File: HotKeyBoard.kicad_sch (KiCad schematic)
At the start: 397 parts, among them J1 Conn_01x04_Pin, J2 Conn_01x20_Pin, J3 Conn_01x20_Pin, J4 Conn_01x02_Socket, J5 Conn_01x02_Socket, J6 Conn_01x02_Socket, Q1 IRLZ34N, Q2 IRLZ34N, Q3 IRLZ34N, SW1 SW_Push, SW10 SW_Push, SW11 SW_Push, SW12 SW_Push, SW13 SW_Push, SW14 SW_Push, SW15 SW_Push, SW16 SW_Push, SW17 SW_Push, SW18 SW_Push, SW19 SW_Push, SW2 SW_Push, SW20 SW_Push, SW21 SW_Push, SW22 SW_Push, SW23 SW_Push, SW24 SW_Push, SW25 SW_Push, SW26 SW_Push, SW27 SW_Push, SW28 SW_Push, SW29 SW_Push, SW3 SW_Push, SW30 SW_Push, SW31 SW_Push, SW32 SW_Push, SW33 SW_Push, SW34 SW_Push, SW35 SW_Push, SW36 SW_Push, SW37 SW_Push, SW38 SW_Push, SW39 SW_Push, SW4 SW_Push, SW40 SW_Push, SW41 SW_Push, SW42 SW_Push, SW43 SW_Push, SW44 SW_Push, SW45 SW_Push, SW46 SW_Push, SW47 SW_Push, SW48 SW_Push, SW49 SW_Push, SW5 SW_Push, SW50 SW_Push, SW51 SW_Push, SW52 SW_Push, SW53 SW_Push, SW54 SW_Push, SW55 SW_Push, SW56 SW_Push, SW57 SW_Push, SW58 SW_Push, SW59 SW_Push, SW6 SW_Push, SW60 SW_Push, SW61 SW_Push, SW62 SW_Push, SW63 SW_Push, SW64 SW_Push, SW65 SW_Push, SW66 SW_Push, SW67 SW_Push, SW68 SW_Push, SW69 SW_Push, SW7 SW_Push, SW70 SW_Push, SW71 SW_Push, SW72 SW_Push, SW76 SW_Push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

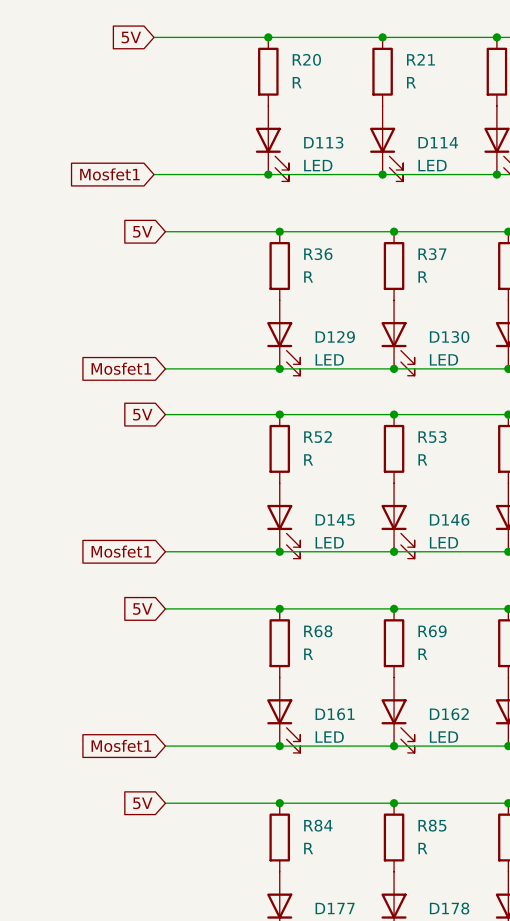
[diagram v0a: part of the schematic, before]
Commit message: Rewired leds
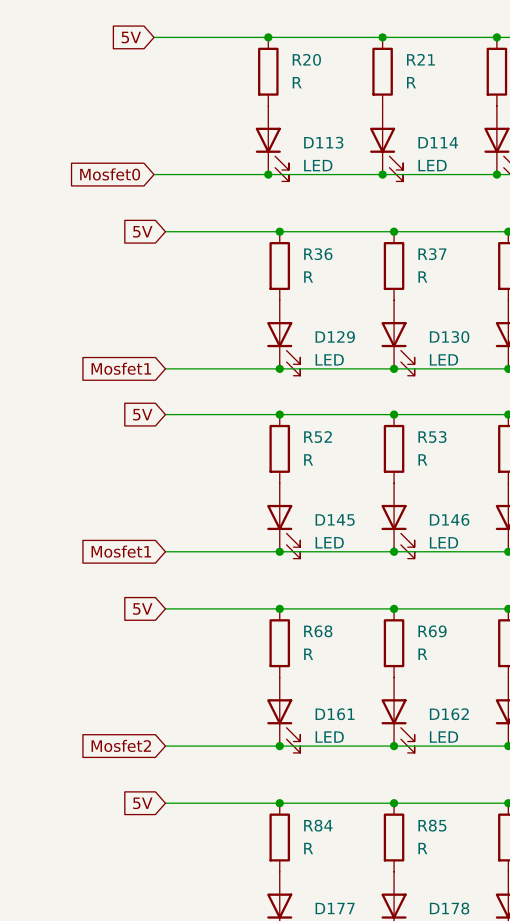
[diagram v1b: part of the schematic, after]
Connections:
- net Mosfet0: now also D113.1 (K), D114.1 (K), D115.1 (K), D116.1 (K), D117.1 (K), D118.1 (K), D119.1 (K), D120.1 (K), D121.1 (K), D122.1 (K), D123.1 (K), D124.1 (K), D125.1 (K), D126.1 (K), D127.1 (K), D128.1 (K)
- net Mosfet1: no longer D113.1 (K), D114.1 (K), D115.1 (K), D116.1 (K), D117.1 (K), D118.1 (K), D119.1 (K), D120.1 (K), D121.1 (K), D122.1 (K), D123.1 (K), D124.1 (K), D125.1 (K), D126.1 (K), D127.1 (K), D128.1 (K), D161.1 (K), D162.1 (K), D163.1 (K), D164.1 (K), D165.1 (K), D166.1 (K), D167.1 (K), D168.1 (K), D169.1 (K), D170.1 (K), D171.1 (K), D172.1 (K), D173.1 (K), D174.1 (K), D175.1 (K), D176.1 (K)
- net Mosfet2: now also D161.1 (K), D162.1 (K), D163.1 (K), D164.1 (K), D165.1 (K), D166.1 (K), D167.1 (K), D168.1 (K), D169.1 (K), D170.1 (K), D171.1 (K), D172.1 (K), D173.1 (K), D174.1 (K), D175.1 (K), D176.1 (K)
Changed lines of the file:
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@@
     )
   )
-  (global_label "Mosfet1" (shape input) (at 62.23 236.22 180)
+  (global_label "Mosfet0" (shape input) (at 62.23 236.22 180)
     (effects (font (size 1.27 1.27)) (justify right))
     (property "Intersheetrefs" "${INTERSHEET_REFS}" (at 62.23 236.22 0)
@@
     )
   )
-  (global_label "Mosfet1" (shape input) (at 63.5 299.72 180)
+  (global_label "Mosfet2" (shape input) (at 63.5 299.72 180)
     (effects (font (size 1.27 1.27)) (justify right))
     (property "Intersheetrefs" "${INTERSHEET_REFS}" (at 63.5 299.72 0)

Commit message: Changed led resistor to smaller value to give pwm control more range to play with
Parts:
- R10, R11, R12, R13, R14, R15, R16, R17, R18, R19, R20, R21, R22, R23, R24, R25, R26, R27, R28, R29, R30, R31, R32, R33, R34, R35, R36, R37, R38, R39, R4, R40, R41, R42, R43, R44, R45, R46, R47, R48, R49, R5, R50, R51, R52, R53, R54, R55, R56, R57, R58, R59, R6, R60, R61, R62, R63, R64, R65, R66, R67, R68, R69, R7, R70, R71, R72, R73, R74, R75, R76, R77, R78, R79, R8, R80, R81, R82, R83, R84, R85, R86, R87, R88, R89, R9, R90, R91, R92, R93, R94, R95, R96, R97, R98, R99: LCSC C881395 -> C101269

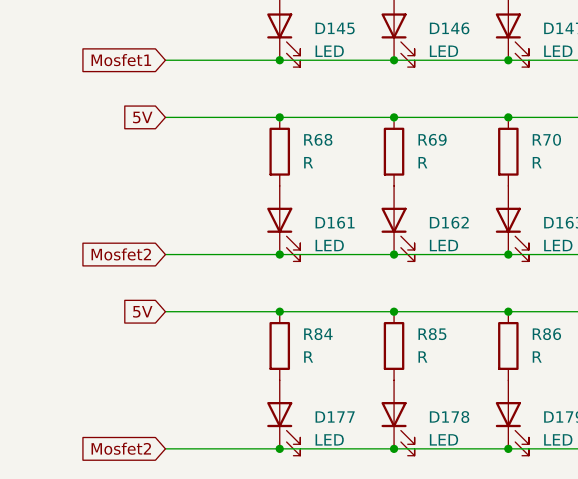
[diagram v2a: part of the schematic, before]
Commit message: Added 0ohm resistor before the last led row in order to be able to turn it off
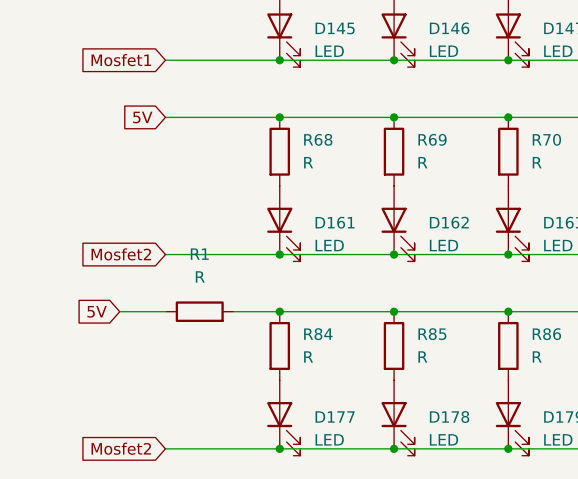
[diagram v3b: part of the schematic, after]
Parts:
- added R1: R, Resistor_THT:R_Axial_DIN0204_L3.6mm_D1.6mm_P5.08mm_Horizontal, symbol Device:R
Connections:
- net 5V: now also R1.1; no longer R84.1, R85.1, R86.1, R87.1, R88.1, R89.1, R90.1, R91.1, R92.1, R93.1, R94.1, R95.1, R96.1, R97.1, R98.1, R99.1
- new net: R1.2, R84.1, R85.1, R86.1, R87.1, R88.1, R89.1, R90.1, R91.1, R92.1, R93.1, R94.1, R95.1, R96.1, R97.1, R98.1, R99.1
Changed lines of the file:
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@@
   (junction (at 485.14 104.14) (diameter 0) (color 0 0 0 0)
   )
-  (junction (at 76.2 306.07) (diameter 0) (color 0 0 0 0)
-  )
   (junction (at 163.83 236.22) (diameter 0) (color 0 0 0 0)
   )
@@
   (junction (at 228.6 306.07) (diameter 0) (color 0 0 0 0)
   )
+  (junction (at 76.2 306.07) (diameter 0) (color 0 0 0 0)
+  )
   (junction (at 353.06 124.46) (diameter 0) (color 0 0 0 0)
   )
@@
     (stroke (width 0) (type default))
   )
+  (wire (pts (xy 58.42 306.07) (xy 63.5 306.07))
+    (stroke (width 0) (type default))
+  )
   (wire (pts (xy 486.41 284.48) (xy 486.41 281.94))
     (stroke (width 0) (type default))
@@
     (stroke (width 0) (type default))
   )
-  (wire (pts (xy 63.5 306.07) (xy 76.2 306.07))
-    (stroke (width 0) (type default))
-  )
   (polyline (pts (xy 521.97 207.01) (xy 528.32 207.01))
     (stroke (width 0) (type default))
@@
     (stroke (width 0) (type default))
   )
+  (wire (pts (xy 71.12 306.07) (xy 76.2 306.07))
+    (stroke (width 0) (type default))
+  )
   (wire (pts (xy 139.7 321.31) (xy 152.4 321.31))
     (stroke (width 0) (type default))
@@
     )
   )
-  (global_label "5V" (shape input) (at 63.5 306.07 180) (fields_autoplaced)
+  (global_label "5V" (shape input) (at 58.42 306.07 180) (fields_autoplaced)
     (effects (font (size 1.27 1.27)) (justify right))
-    (property "Intersheetrefs" "${INTERSHEET_REFS}" (at 58.2167 306.07 0)
+    (property "Intersheetrefs" "${INTERSHEET_REFS}" (at 53.1367 306.07 0)
       (effects (font (size 1.27 1.27)) (justify right) hide)
     )
@@
         )
       )
+    )
+  )
+  (symbol (lib_id "Device:R") (at 67.31 306.07 90) (unit 1)
+    (in_bom yes) (on_board yes) (dnp no) (fields_autoplaced)
+    (property "Reference" "R1" (at 67.31 299.72 90)
+      (effects (font (size 1.27 1.27)))
+    )
+    (property "Value" "R" (at 67.31 302.26 90)
+      (effects (font (size 1.27 1.27)))
+    )
+    (property "Footprint" "Resistor_THT:R_Axial_DIN0204_L3.6mm_D1.6mm_P5.08mm_Horizontal" (at 67.31 307.848 90)
+      (effects (font (size 1.27 1.27)) hide)
+    )
+    (property "Datasheet" "~" (at 67.31 306.07 0)
+      (effects (font (size 1.27 1.27)) hide)
+    )
+    (pin "1")
+    (pin "2")
+    (instances
+      (project "HotKeyBoard"
+        (path "/ad7237f5-a3d9-4e9d-bcab-b0d3445713fa"
+          (reference "R1") (unit 1)
+        )
+      )
